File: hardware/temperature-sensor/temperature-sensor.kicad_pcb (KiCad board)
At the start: 2 copper layers, 56 x 56 mm, 126 parts, among them IC1 SHT40-CD1B-R3, IC2 MAX5969BETB+T, IC3 LV2862XLVDDCR, IC4 LV2862XLVDDCR, J1 1149611, J2 219320-0001, J3 1990012, J4 ARM-JTAG-SWD, Q1 DMN3404L, Q2 DMN3404L, Q3 DMN3404L, Q4 DMN3404L, T1 SM13126PEL, U1 STM32F407V_E-G_Tx, U2 LAN8720A, U3 FT230XS, U4 AT24C512C, Y1 CX2016FB25000C0FZZH1

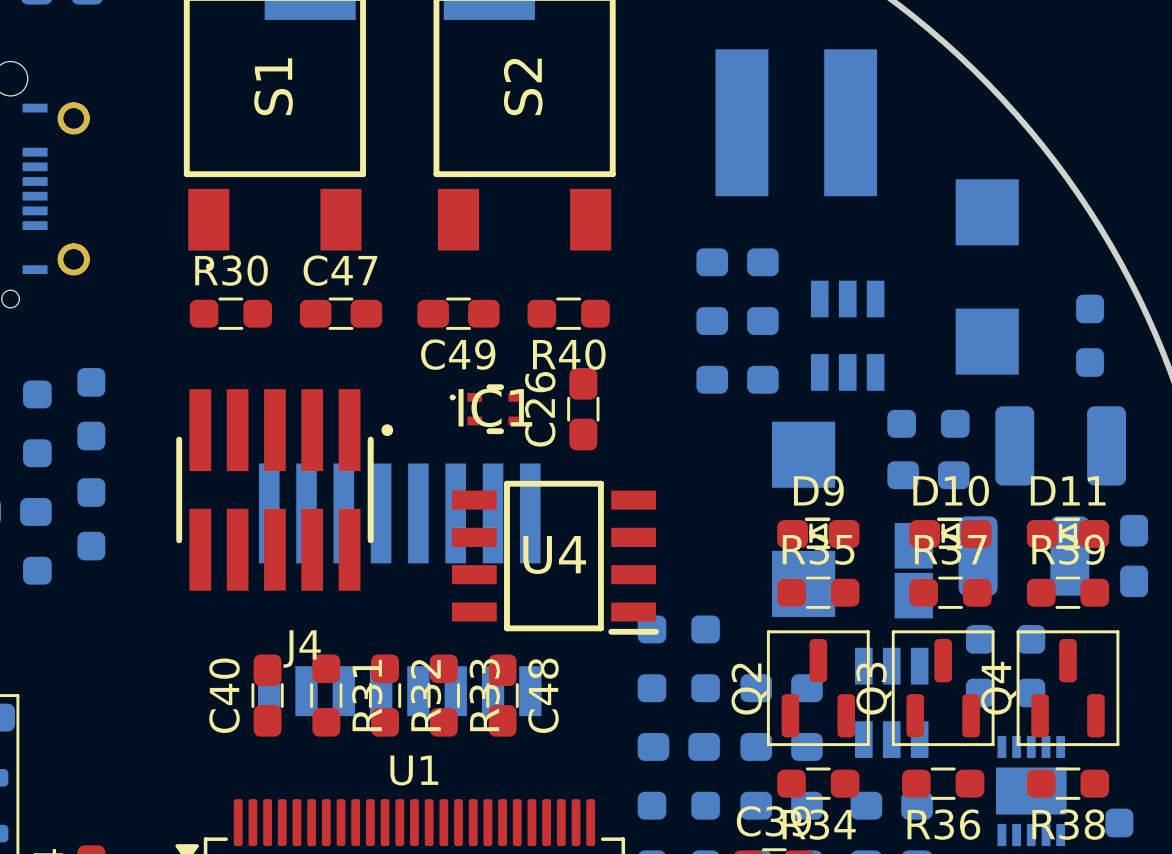
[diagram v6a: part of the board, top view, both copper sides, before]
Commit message: improve placement of temperature sensor
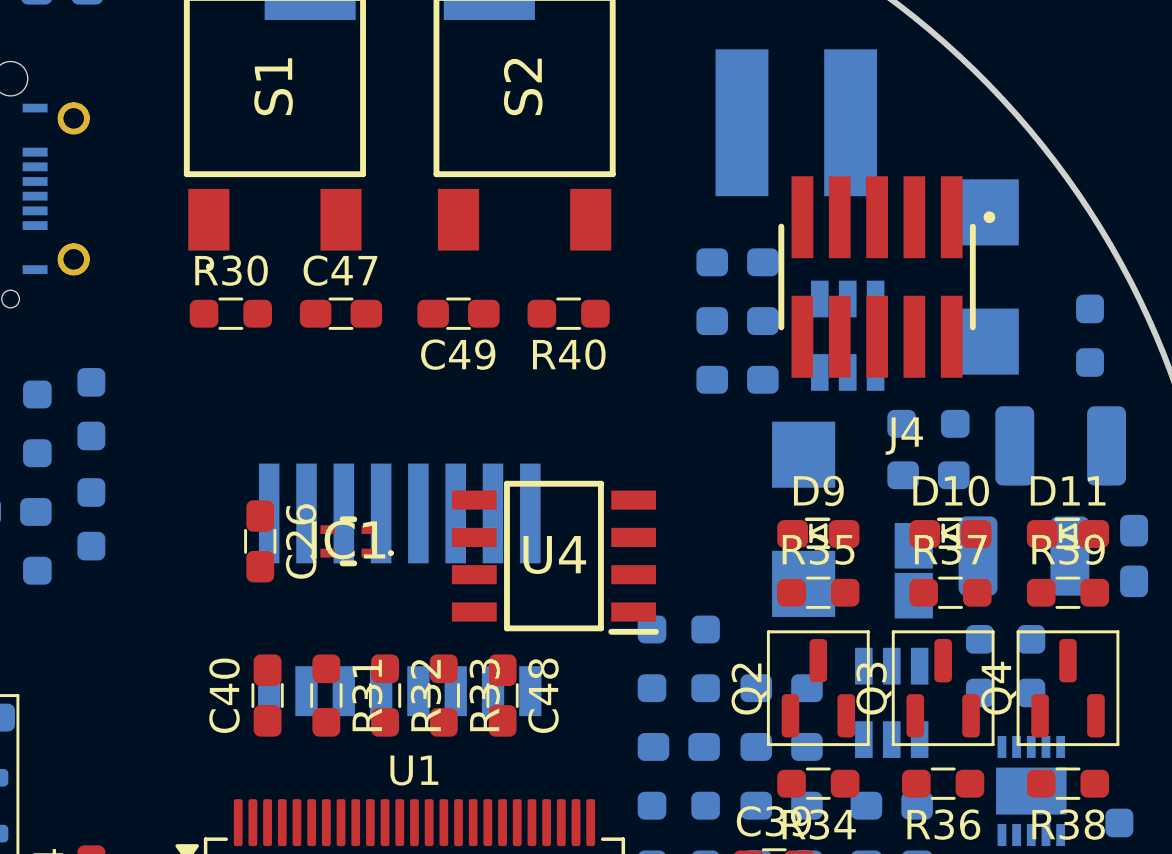
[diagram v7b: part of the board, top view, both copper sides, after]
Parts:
- moved J4 21.7 mm to (166.2, 86.0)
- moved C26 11.9 mm to (145.2, 95.0), turned to -90 degrees
- moved IC1 6.73 mm to (148.2, 95.0), turned to 180 degrees
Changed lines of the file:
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@@
 		(placed yes)
 		(layer "F.Cu")
-		(at 156.25 90.5 90)
+		(at 145.25 95 -90)
 		(descr "Capacitor SMD 0603 (1608 Metric), square (rectangular) end terminal, IPC_7351 nominal with elongated pad for handsoldering. (Body size source: IPC-SM-782 page 76, https://www.pcb-3d.com/wordpress/wp-content/uploads/ipc-sm-782a_amendment_1_and_2.pdf), generated with kicad-footprint-generator")
 		(tags "capacitor handsolder")
@@
 		)
 		(property "RS order number" "242-7372"
-			(at 0 0 90)
+			(at 0 0 -90)
 			(unlocked yes)
 			(layer "F.Fab")
@@
 		)
 		(property "Mouser Part Number" "581-KGM15BR71H104KM"
-			(at 0 0 90)
+			(at 0 0 -90)
 			(unlocked yes)
 			(layer "F.Fab")
@@
 		(attr smd)
 		(fp_line
-			(start -0.375 -0.5)
-			(end 0.375 -0.5)
+			(start -0.375 0.5)
+			(end 0.375 0.5)
 			(stroke
 				(width 0.1)
@@
 		)
 		(fp_line
-			(start -0.375 0.5)
-			(end 0.375 0.5)
+			(start -0.375 -0.5)
+			(end 0.375 -0.5)
 			(stroke
 				(width 0.1)
@@
 		)
 		(fp_line
-			(start 1.65 -0.73)
-			(end 1.65 0.73)
+			(start -1.65 0.73)
+			(end -1.65 -0.73)
 			(stroke
 				(width 0.05)
@@
 		)
 		(fp_line
-			(start -1.65 -0.73)
-			(end 1.65 -0.73)
+			(start 1.65 0.73)
+			(end -1.65 0.73)
 			(stroke
 				(width 0.05)
@@
 		)
 		(fp_line
-			(start 1.65 0.73)
-			(end -1.65 0.73)
+			(start -1.65 -0.73)
+			(end 1.65 -0.73)
 			(stroke
 				(width 0.05)
@@
 		)
 		(fp_line
-			(start -1.65 0.73)
-			(end -1.65 -0.73)
+			(start 1.65 -0.73)
+			(end 1.65 0.73)
 			(stroke
 				(width 0.05)
@@
 		)
 		(fp_line
-			(start 0.8 -0.4)
-			(end 0.8 0.4)
+			(start -0.8 0.4)
+			(end -0.8 -0.4)
 			(stroke
 				(width 0.1)
@@
 		)
 		(fp_line
-			(start -0.8 -0.4)
-			(end 0.8 -0.4)
+			(start 0.8 0.4)
+			(end -0.8 0.4)
 			(stroke
 				(width 0.1)
@@
 		)
 		(fp_line
-			(start 0.8 0.4)
-			(end -0.8 0.4)
+			(start -0.8 -0.4)
+			(end 0.8 -0.4)
 			(stroke
 				(width 0.1)
@@
 		)
 		(fp_line
-			(start -0.8 0.4)
-			(end -0.8 -0.4)
+			(start 0.8 -0.4)
+			(end 0.8 0.4)
 			(stroke
 				(width 0.1)
@@
 		)
 		(pad "1" smd roundrect
-			(at -0.8625 0 90)
+			(at -0.8625 0 270)
 			(size 1.075 0.95)
 			(layers "F.Cu" "F.Paste" "F.Mask")
@@
 		)
 		(pad "2" smd roundrect
-			(at 0.8625 0 90)
+			(at 0.8625 0 270)
 			(size 1.075 0.95)
 			(layers "F.Cu" "F.Paste" "F.Mask")
@@
 	(footprint "benediktibk:SAMTEC_FTSH-105-01-F-DV-P-TR"
 		(layer "F.Cu")
-		(at 145.75 93.25 180)
+		(at 166.25 86 180)
 		(property "Reference" "J4"
 			(at -1 -5.315 360)
@@
 		(placed yes)
 		(layer "F.Cu")
-		(at 153.25 90.5)
+		(at 148.25 95 180)
 		(descr "SHT40-CD1B-R3-3")
 		(tags "Integrated Circuit")
 		(property "Reference" "IC1"
-			(at 0 0 0)
+			(at 0 0 360)
 			(layer "F.SilkS")
 			(effects
@@
 		)
 		(property "Value" "SHT40-CD1B-R3"
-			(at 0 0 0)
+			(at 0 0 360)
 			(layer "F.SilkS")
 			(hide yes)
@@
 		)
 		(property "Footprint" "benediktibk:SHT40CD1BR3"
-			(at 0 0 0)
+			(at 0 0 360)
 			(layer "F.Fab")
 			(hide yes)
@@
 		)
 		(property "Datasheet" "https://sensirion.com/media/documents/33FD6951/6555C40E/Sensirion_Datasheet_SHT4x.pdf"
-			(at 0 0 0)
+			(at 0 0 360)
 			(layer "F.Fab")
 			(hide yes)
@@
 		)
 		(property "Description" "Board Mount Humidity Sensors +/-1.8%RH/+/-0.2C, 4th generation, digital (I2C) humidity and temperature sensor with 0x46 I2C address."
-			(at 0 0 0)
+			(at 0 0 360)
 			(layer "F.Fab")
 			(hide yes)
@@
 		)
 		(property "Height" "0.59"
-			(at 0 0 0)
+			(at 0 0 180)
 			(unlocked yes)
 			(layer "F.Fab")
@@
 		)
 		(property "Mouser Part Number" "403-SHT40-CD1B-R3"
-			(at 0 0 0)
+			(at 0 0 180)
 			(unlocked yes)
 			(layer "F.Fab")
@@
 		)
 		(property "Mouser Price/Stock" "https://www.mouser.co.uk/ProductDetail/Sensirion/SHT40-CD1B-R3?qs=ulEaXIWI0c%2FeyXO6eo5KrQ%3D%3D"
-			(at 0 0 0)
+			(at 0 0 180)
 			(unlocked yes)
 			(layer "F.Fab")
@@
 		)
 		(property "Manufacturer_Name" "Sensirion"
-			(at 0 0 0)
+			(at 0 0 180)
 			(unlocked yes)
 			(layer "F.Fab")
@@
 		)
 		(property "Manufacturer_Part_Number" "SHT40-CD1B-R3"
-			(at 0 0 0)
+			(at 0 0 180)
 			(unlocked yes)
 			(layer "F.Fab")
@@
 		(attr smd)
 		(fp_line
-			(start -1.5 -0.4)
-			(end -1.5 -0.4)
-			(stroke
-				(width 0.1)
-				(type solid)
-			)
-			(layer "F.SilkS")
-		)
-		(fp_line
-			(start -1.4 -0.4)
-			(end -1.4 -0.4)
+			(start 0.2 0.75)
+			(end -0.2 0.75)
 			(stroke
-				(width 0.1)
+				(width 0.2)
 				(type solid)
 			)
@@
 		)
 		(fp_line
-			(start 0.2 0.75)
-			(end -0.2 0.75)
+			(start -1.4 -0.4)
+			(end -1.4 -0.4)
 			(stroke
-				(width 0.2)
+				(width 0.1)
 				(type solid)
 			)
 			(layer "F.SilkS")
 		)
-		(fp_arc
+		(fp_line
 			(start -1.5 -0.4)
-			(mid -1.45 -0.45)
-			(end -1.4 -0.4)
+			(end -1.5 -0.4)
 			(stroke
 				(width 0.1)
@@
 			(layer "F.SilkS")
 		)
-		(fp_line
-			(start -1.95 -1.75)
-			(end 1.95 -1.75)
+		(fp_arc
+			(start -1.5 -0.4)
+			(mid -1.45 -0.45)
+			(end -1.4 -0.4)
 			(stroke
 				(width 0.1)
 				(type solid)
 			)
-			(layer "F.CrtYd")
+			(layer "F.SilkS")
 		)
 		(fp_line
-			(start -1.95 1.75)
-			(end -1.95 -1.75)
+			(start 1.95 1.75)
+			(end -1.95 1.75)
 			(stroke
 				(width 0.1)
@@
 		)
 		(fp_line
-			(start 1.95 1.75)
-			(end -1.95 1.75)
+			(start -1.95 1.75)
+			(end -1.95 -1.75)
 			(stroke
 				(width 0.1)
@@
 		)
 		(fp_line
-			(start -0.75 -0.75)
-			(end 0.75 -0.75)
+			(start -1.95 -1.75)
+			(end 1.95 -1.75)
 			(stroke
 				(width 0.1)
 				(type solid)
 			)
-			(layer "F.Fab")
+			(layer "F.CrtYd")
 		)
 		(fp_line
-			(start -0.75 0.75)
-			(end -0.75 -0.75)
+			(start 0.75 0.75)
+			(end -0.75 0.75)
 			(stroke
 				(width 0.1)
@@
 		)
 		(fp_line
-			(start 0.75 0.75)
-			(end -0.75 0.75)
+			(start -0.75 0.75)
+			(end -0.75 -0.75)
+			(stroke
+				(width 0.1)
+				(type solid)
+			)
+			(layer "F.Fab")
+		)
+		(fp_line
+			(start -0.75 -0.75)
+			(end 0.75 -0.75)
 			(stroke
 				(width 0.1)
@@
 		)
 		(fp_text user "${REFERENCE}"
-			(at 0 0 0)
+			(at 0 0 360)
 			(layer "F.Fab")
 			(effects
@@
 		)
 		(pad "1" smd rect
-			(at -0.7 -0.4 90)
+			(at -0.7 -0.4 270)
 			(size 0.3 0.5)
 			(layers "F.Cu" "F.Paste" "F.Mask")
@@
 		)
 		(pad "2" smd rect
-			(at -0.7 0.4 90)
+			(at -0.7 0.4 270)
 			(size 0.3 0.5)
 			(layers "F.Cu" "F.Paste" "F.Mask")
@@
 		)
 		(pad "3" smd rect
-			(at 0.7 0.4 90)
+			(at 0.7 0.4 270)
 			(size 0.3 0.5)
 			(layers "F.Cu" "F.Paste" "F.Mask")
@@
 		)
 		(pad "4" smd rect
-			(at 0.7 -0.4 90)
+			(at 0.7 -0.4 270)
 			(size 0.3 0.5)
 			(layers "F.Cu" "F.Paste" "F.Mask")

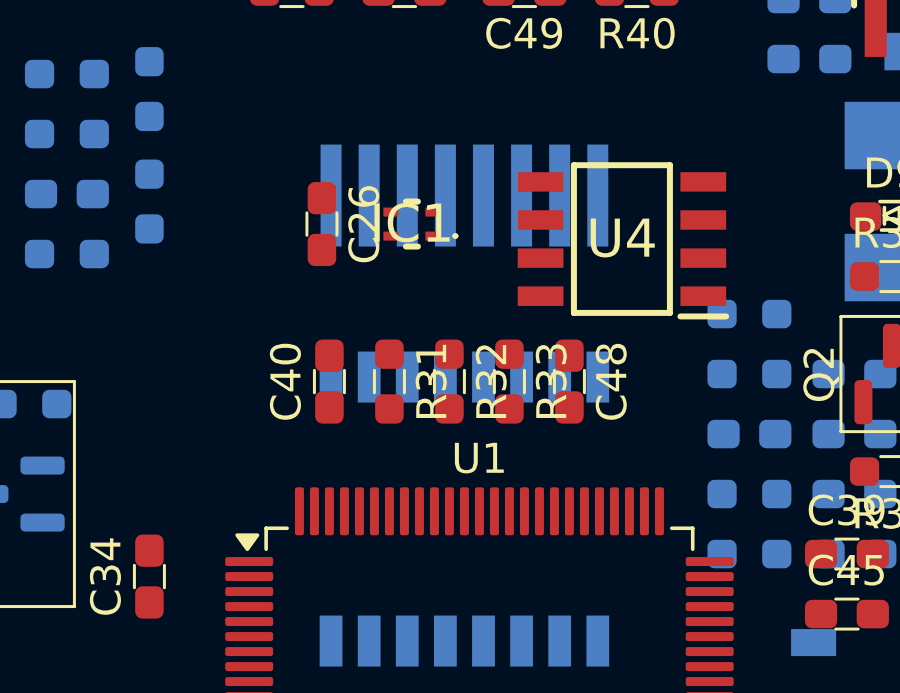
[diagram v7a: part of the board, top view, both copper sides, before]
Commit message: define layers for routing
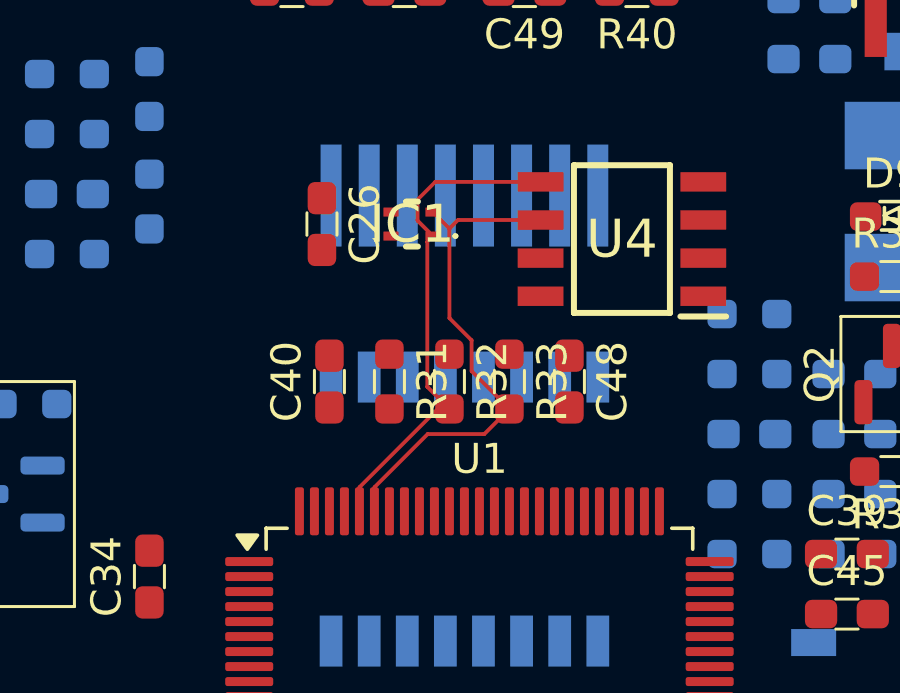
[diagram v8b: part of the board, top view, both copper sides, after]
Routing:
- net /MCU/SCL: track 0.00 -> 17.2 mm
- net /MCU/SDA: track 0.00 -> 16.8 mm
- added copper zone on In2.Cu, net GND
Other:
- copper layers 2 -> 4
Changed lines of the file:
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@@
 	(layers
 		(0 "F.Cu" signal)
+		(1 "In1.Cu" power "Supply")
+		(2 "In2.Cu" power "GND")
 		(31 "B.Cu" signal)
 		(32 "B.Adhes" user "B.Adhesive")
@@
 	)
 	(setup
+		(stackup
+			(layer "F.SilkS"
+				(type "Top Silk Screen")
+			)
+			(layer "F.Paste"
+				(type "Top Solder Paste")
+			)
+			(layer "F.Mask"
+				(type "Top Solder Mask")
+				(thickness 0.01)
+			)
+			(layer "F.Cu"
+				(type "copper")
+				(thickness 0.035)
+			)
+			(layer "dielectric 1"
+				(type "prepreg")
+				(thickness 0.1)
+				(material "FR4")
+				(epsilon_r 4.5)
+				(loss_tangent 0.02)
+			)
+			(layer "In1.Cu"
+				(type "copper")
+				(thickness 0.035)
+			)
+			(layer "dielectric 2"
+				(type "core")
+				(thickness 1.24)
+				(material "FR4")
+				(epsilon_r 4.5)
+				(loss_tangent 0.02)
+			)
+			(layer "In2.Cu"
+				(type "copper")
+				(thickness 0.035)
+			)
+			(layer "dielectric 3"
+				(type "prepreg")
+				(thickness 0.1)
+				(material "FR4")
+				(epsilon_r 4.5)
+				(loss_tangent 0.02)
+			)
+			(layer "B.Cu"
+				(type "copper")
+				(thickness 0.035)
+			)
+			(layer "B.Mask"
+				(type "Bottom Solder Mask")
+				(thickness 0.01)
+			)
+			(layer "B.Paste"
+				(type "Bottom Solder Paste")
+			)
+			(layer "B.SilkS"
+				(type "Bottom Silk Screen")
+			)
+			(copper_finish "None")
+			(dielectric_constraints no)
+		)
 		(pad_to_mask_clearance 0)
 		(allow_soldermask_bridges_in_footprints no)
@@
 		)
 	)
+	(segment
+		(start 148.4365 94.1865)
+		(end 148.4365 94.8865)
+		(width 0.127)
+		(layer "F.Cu")
+		(net 6)
+	)
+	(segment
+		(start 148.7615 95.5885)
+		(end 148.7615 100.424)
+		(width 0.127)
+		(layer "F.Cu")
+		(net 6)
+	)
+	(segment
+		(start 152.538 93.595)
+		(end 149.028 93.595)
+		(width 0.127)
+		(layer "F.Cu")
+		(net 6)
+	)
+	(segment
+		(start 148.4365 94.8865)
+		(end 148.95 95.4)
+		(width 0.127)
+		(layer "F.Cu")
+		(net 6)
+	)
+	(segment
+		(start 149.112501 101.1625)
+		(end 149.5 101.1625)
+		(width 0.127)
+		(layer "F.Cu")
+		(net 6)
+	)
+	(segment
+		(start 146.5 104.575)
+		(end 146.5 103.775001)
+		(width 0.127)
+		(layer "F.Cu")
+		(net 6)
+	)
+	(segment
+		(start 148.7615 100.424)
+		(end 149.5 101.1625)
+		(width 0.127)
+		(layer "F.Cu")
+		(net 6)
+	)
+	(segment
+		(start 146.5 103.775001)
+		(end 149.112501 101.1625)
+		(width 0.127)
+		(layer "F.Cu")
+		(net 6)
+	)
+	(segment
+		(start 149.028 93.595)
+		(end 148.4365 94.1865)
+		(width 0.127)
+		(layer "F.Cu")
+		(net 6)
+	)
+	(segment
+		(start 148.95 95.4)
+		(end 148.7615 95.5885)
+		(width 0.127)
+		(layer "F.Cu")
+		(net 6)
+	)
+	(segment
+		(start 150.6625 102)
+		(end 151.5 101.1625)
+		(width 0.127)
+		(layer "F.Cu")
+		(net 90)
+	)
+	(segment
+		(start 149.5 95.15)
+		(end 149.5 98.134898)
+		(width 0.127)
+		(layer "F.Cu")
+		(net 90)
+	)
+	(segment
+		(start 152.538 94.865)
+		(end 149.785 94.865)
+		(width 0.127)
+		(layer "F.Cu")
+		(net 90)
+	)
+	(segment
+		(start 149.5 98.134898)
+		(end 150.2385 98.873398)
+		(width 0.127)
+		(layer "F.Cu")
+		(net 90)
+	)
+	(segment
+		(start 147 103.775001)
+		(end 148.775001 102)
+		(width 0.127)
+		(layer "F.Cu")
+		(net 90)
+	)
+	(segment
+		(start 148.775001 102)
+		(end 150.6625 102)
+		(width 0.127)
+		(layer "F.Cu")
+		(net 90)
+	)
+	(segment
+		(start 150.2385 99.901)
+		(end 151.5 101.1625)
+		(width 0.127)
+		(layer "F.Cu")
+		(net 90)
+	)
+	(segment
+		(start 150.2385 98.873398)
+		(end 150.2385 99.901)
+		(width 0.127)
+		(layer "F.Cu")
+		(net 90)
+	)
+	(segment
+		(start 149.785 94.865)
+		(end 149.5 95.15)
+		(width 0.127)
+		(layer "F.Cu")
+		(net 90)
+	)
+	(segment
+		(start 148.95 94.6)
+		(end 149.5 95.15)
+		(width 0.127)
+		(layer "F.Cu")
+		(net 90)
+	)
+	(segment
+		(start 147 104.575)
+		(end 147 103.775001)
+		(width 0.127)
+		(layer "F.Cu")
+		(net 90)
+	)
+	(zone
+		(net 1)
+		(net_name "GND")
+		(layer "In2.Cu")
+		(hatch edge 0.5)
+		(connect_pads
+			(clearance 0.5)
+		)
+		(min_thickness 0.25)
+		(filled_areas_thickness no)
+		(fill yes
+			(thermal_gap 0.5)
+			(thermal_bridge_width 0.5)
+		)
+		(polygon
+			(pts
+				(xy 120 70) (xy 180 70) (xy 180 130) (xy 120 130)
+			)
+		)
+	)
